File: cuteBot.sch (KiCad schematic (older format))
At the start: 18 parts

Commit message: Añadidos algunos componentes principales
Añadidos los leds. puente en H y pulsador.
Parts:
- removed U?: ATMEGA32U4-MU, QFN44, symbol atmel:ATMEGA32U4-MU
- added C10: 10uF, symbol device:CP_Small
- added C11: 0.01uF, symbol device:C_Small
- added C12, C13, C14, C15, C16: 100nF, symbol device:C_Small
- added C3, C4: 22uF, symbol device:C_Small
- added C5, C6: 22pF, symbol device:C_Small
- added C7: 1uF, symbol device:C_Small
- added C8: 100n, symbol device:C_Small
- added C9: 2.2uF, symbol device:C_Small
- added D3: SS34, symbol device:D_Schottky_Small
- added D4: GREEN, symbol device:LED_Small_ALT
- added D5: RED, symbol device:LED_Small_ALT
- added L1: 22nH, symbol device:L_Small
- added LED1, LED2, LED3, LED4, LED5: WS2812B, LEDs:LED_WS2812B-PLCC4, symbol Worldsemi:WS2812B
- added P4: MOTOR_A, symbol conn:CONN_01X02
- added P5: MOTOR_B, symbol conn:CONN_01X02
- added R10, R15: 10k, symbol device:R_Small
- added R11, R12: 0.2R, symbol device:R_Small
- added R13, R14: 330, symbol device:R_Small
- added R6: 7.5K, symbol device:R_Small
- added R7: 1K, symbol device:R_Small
- added R8, R9: 22R, symbol device:R_Small
- added SW2: SW_Push, symbol Switch:SW_Push
- added U1: ATMEGA32U4-MU, QFN44, symbol atmel:ATMEGA32U4-MU
- added U6: DRV8833RTY, Housings_DFN_QFN:WQFN-16-1EP_4x4mm_Pitch0.65mm, symbol motor_drivers:DRV8833RTY
- added Y1: 16MHz, symbol device:Crystal_Small
- R1: renamed from R?; value 2K -> 4k
- gave numbers to parts that had none: 16
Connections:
- net labels added: 5V, AREF, B1, D+, D-, MOTOR_A_1, MOTOR_A_2, MOTOR_B_1, MOTOR_B_2, NEO, RX_LED, TX_LED, VCP
- wire segments 62 -> 245
- no-connect marks 4 -> 7

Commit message: Añadiendo los componentes, hay algunos errores de footprint
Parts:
- added BZ1: Buzzer, Buzzers_Beepers:PUIAudio_SMT_0825_S_4_R, symbol device:Buzzer
- added C17: 470pF, Capacitors_SMD:C_0603, symbol device:C_Small
- added C18: 2.2uF, Capacitors_SMD:C_0603, symbol device:CP_Small
- added C19, C20: 0.1uF, Capacitors_SMD:C_0603, symbol device:C_Small
- added C21: 10uF, Capacitors_SMD:C_0603, symbol device:C_Small
- added D6: 1N4148, Diodes_SMD:D_MicroMELF, symbol Diode:1N4148
- added P6: CONN_02X03, Connectors:2X3_SMT_POSTS, symbol conn:CONN_02X03
- added Q1: S8050, TO_SOT_Packages_THT:TO-92_Molded_Narrow, symbol Transistor:S8050
- added R16: 100, Resistors_SMD:R_0603, symbol device:R_Small
- added SW3: SW_Push, Buttons_Switches_SMD:SW_SPST_B3U-3000P, symbol Switch:SW_Push
- added U7: JDY-08, JDY-08:JDY-08, symbol jdy-08:JDY-08
- added U8: MIC5219-3.3, TO_SOT_Packages_SMD:SOT-23-5, symbol regul:MIC5219-3.3
- C1, C10, C11, C12, C13, C14, C15, C16, C2, C5, C6, C7, C8, C9: footprint (none) -> Capacitors_SMD:C_0603
- C3, C4: footprint (none) -> Capacitors_SMD:C_1812
- D1, D2, D4, D5: footprint (none) -> LEDs:LED_0603
- D3: footprint (none) -> Diodes_SMD:D_SMA
- L1: footprint (none) -> Inductors_SMD:L_7.3x7.3_H4.5
- LED1, LED2, LED3, LED4, LED5: footprint LEDs:LED_WS2812B-PLCC4 -> LED:LED_SK6812MINI_PLCC4_3.5x3.5mm_P1.75mm
- P1: footprint (none) -> Connectors_USB:USB_Micro-B_Molex-105017-0001
- P2, P3: footprint (none) -> Connectors_TestPoints:Test_Point_Pad_d1.0mm
- P4, P5: footprint (none) -> Connectors_JST:JST_PH_B2B-PH-SM4-TB_02x2.00mm_Straight
- R1, R10, R11, R12, R13, R14, R15, R2, R3, R4, R5, R6, R7, R8, R9: footprint (none) -> Resistors_SMD:R_0603
- SW1: footprint (none) -> Buttons_Switches_SMD:SW_SPDT_PCM12
- SW2: footprint (none) -> Buttons_Switches_SMD:SW_SPST_B3U-3000P
- U1: footprint QFN44 -> Housings_DFN_QFN:QFN-44-1EP_7x7mm_Pitch0.5mm
- U2: footprint (none) -> Housings_SOIC:HTSOP-8-1EP_3.9x4.9mm_Pitch1.27mm_ThermalVias
- U3, U4, U5: footprint (none) -> TO_SOT_Packages_SMD:SOT-23-6
- Y1: footprint (none) -> Crystals:Resonator_7.2x3mm
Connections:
- net labels added: 3.3V, BUZZ, MISO, MOSI, RST, RXD, SCK, TXD
- wire segments 245 -> 302
- no-connect marks 7 -> 25
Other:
- note added: "No conectar las resistencias\na menos que se quiera limitar \nla corriente de los motores"
- moved on the sheet: SW2

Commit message: Footprints correctos
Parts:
- BZ1: footprint Buzzers_Beepers:PUIAudio_SMT_0825_S_4_R -> frizzy_switches:Buzzer-7.5x7.5mm
- P4, P5: footprint Connectors_JST:JST_PH_B2B-PH-SM4-TB_02x2.00mm_Straight -> frizzy_switches:SMD_2pin_Solderpad
- Y1: footprint Crystals:Resonator_7.2x3mm -> Clocks:RESONATOR-SMD-3.2X1.3
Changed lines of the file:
@@
 F 0 "Y1" V 1454 4263 50  0000 R CNN
 F 1 "16MHz" V 1545 4263 50  0000 R CNN
-F 2 "Crystals:Resonator_7.2x3mm" H 1500 4350 50  0001 C CNN
+F 2 "Clocks:RESONATOR-SMD-3.2X1.3" H 1500 4350 50  0001 C CNN
 F 3 "" H 1500 4350 50  0001 C CNN
 	1    1500 4350
@@
 F 0 "P4" H 10728 5541 50  0000 L CNN
 F 1 "MOTOR_A" H 10728 5450 50  0000 L CNN
-F 2 "Connectors_JST:JST_PH_B2B-PH-SM4-TB_02x2.00mm_Straight" H 10650 5500 50  0001 C CNN
+F 2 "frizzy_switches:SMD_2pin_Solderpad" H 10650 5500 50  0001 C CNN
 F 3 "" H 10650 5500 50  0001 C CNN
 	1    10650 5500
@@
 F 0 "P5" H 10727 5841 50  0000 L CNN
 F 1 "MOTOR_B" H 10727 5750 50  0000 L CNN
-F 2 "Connectors_JST:JST_PH_B2B-PH-SM4-TB_02x2.00mm_Straight" H 10650 5800 50  0001 C CNN
+F 2 "frizzy_switches:SMD_2pin_Solderpad" H 10650 5800 50  0001 C CNN
 F 3 "" H 10650 5800 50  0001 C CNN
 	1    10650 5800
@@
 F 0 "BZ1" H 9103 3279 50  0000 L CNN
 F 1 "Buzzer" H 9103 3188 50  0000 L CNN
-F 2 "Buzzers_Beepers:PUIAudio_SMT_0825_S_4_R" V 8925 3350 50  0001 C CNN
+F 2 "frizzy_switches:Buzzer-7.5x7.5mm" V 8925 3350 50  0001 C CNN
 F 3 "" V 8925 3350 50  0001 C CNN
 	1    8950 3250

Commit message: Colocando los componentes
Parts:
- Q1: footprint TO_SOT_Packages_THT:TO-92_Molded_Narrow -> TO_SOT_Packages_SMD:SOT-23
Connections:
- wire segments 302 -> 303
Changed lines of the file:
@@
 F 0 "Q1" H 8941 3696 50  0000 L CNN
 F 1 "S8050" H 8941 3605 50  0000 L CNN
-F 2 "TO_SOT_Packages_THT:TO-92_Molded_Narrow" H 8950 3575 50  0001 L CIN
+F 2 "TO_SOT_Packages_SMD:SOT-23" H 8950 3575 50  0001 L CIN
 F 3 "http://www.unisonic.com.tw/datasheet/S8050.pdf" H 8750 3650 50  0001 L CNN
 	1    8750 3650
@@
 Wire Wire Line
 	1200 3850 1450 3850
+Text GLabel 4050 5050 2    50   Input ~ 0
+BUZZ
+Wire Wire Line
+	3950 5050 4050 5050
 $EndSCHEMATC

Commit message: Colocando los componentes
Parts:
- BZ1: symbol device:Buzzer -> cuteBot-rescue:Buzzer-device
- C1, C11, C12, C13, C14, C15, C16, C17, C19, C2, C20, C21, C3, C4, C5, C6, C7, C8, C9: symbol device:C_Small -> cuteBot-rescue:C_Small-device
- C10, C18: symbol device:CP_Small -> cuteBot-rescue:CP_Small-device
- D1, D2, D4, D5: symbol device:LED_Small_ALT -> cuteBot-rescue:LED_Small_ALT-device
- D3: symbol device:D_Schottky_Small -> cuteBot-rescue:D_Schottky_Small-device
- L1: symbol device:L_Small -> cuteBot-rescue:L_Small-device
- LED1, LED2, LED3, LED4, LED5: symbol Worldsemi:WS2812B -> cuteBot-rescue:WS2812B-Worldsemi
- P1: symbol conn:USB_A -> cuteBot-rescue:USB_A-conn
- P2, P3: symbol conn:CONN_01X01 -> cuteBot-rescue:CONN_01X01-conn
- P4, P5: symbol conn:CONN_01X02 -> cuteBot-rescue:CONN_01X02-conn
- P6: symbol conn:CONN_02X03 -> cuteBot-rescue:CONN_02X03-conn
- Q1: symbol Transistor:S8050 -> cuteBot-rescue:S8050-Transistor
- R1, R10, R11, R12, R13, R14, R15, R16, R2, R3, R4, R5, R6, R7, R8, R9: symbol device:R_Small -> cuteBot-rescue:R_Small-device
- U1: symbol atmel:ATMEGA32U4-MU -> cuteBot-rescue:ATMEGA32U4-MU-atmel
- U2: symbol tp4056:TP4056 -> cuteBot-rescue:TP4056-tp4056
- U3: symbol frizzy_ICs:FS312F-G -> cuteBot-rescue:FS312F-G-frizzy_ICs
- U4: symbol frizzy_ICs:FS8205 -> cuteBot-rescue:FS8205-frizzy_ICs
- U5: symbol frizzy_ICs:MT3608 -> cuteBot-rescue:MT3608-frizzy_ICs
- U6: symbol motor_drivers:DRV8833RTY -> cuteBot-rescue:DRV8833RTY-motor_drivers
- U7: symbol jdy-08:JDY-08 -> cuteBot-rescue:JDY-08-jdy-08
- U8: symbol regul:MIC5219-3.3 -> cuteBot-rescue:MIC5219-3.3-regul
- Y1: symbol device:Crystal_Small -> cuteBot-rescue:Crystal_Small-device

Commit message: Resonador cambiado
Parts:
- removed C5, C6: 22pF, Capacitors_SMD:C_0603, symbol cuteBot-rescue:C_Small-device
- Y1: symbol cuteBot-rescue:Crystal_Small-device -> device:Resonator_Small
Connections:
- net GND: now also Y1.2
- net at U1.16 (XTAL2): now also Y1.3; no longer Y1.2
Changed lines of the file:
@@
 $EndComp
 $Comp
-L cuteBot-rescue:Crystal_Small-device Y1
+L device:Resonator_Small Y1
 U 1 1 5C2CFA66
-P 1500 4350
-F 0 "Y1" V 1454 4263 50  0000 R CNN
-F 1 "16MHz" V 1545 4263 50  0000 R CNN
-F 2 "Clocks:RESONATOR-SMD-3.2X1.3" H 1500 4350 50  0001 C CNN
-F 3 "" H 1500 4350 50  0001 C CNN
-	1    1500 4350
-	0    1    1    0
-$EndComp
-$Comp
-L cuteBot-rescue:C_Small-device C5
-U 1 1 5C2CFD53
-P 1300 4200
-F 0 "C5" V 1071 4200 50  0000 C CNN
-F 1 "22pF" V 1162 4200 50  0000 C CNN
-F 2 "Capacitors_SMD:C_0603" H 1300 4200 50  0001 C CNN
-F 3 "" H 1300 4200 50  0001 C CNN
-	1    1300 4200
-	0    1    1    0
-$EndComp
-$Comp
-L cuteBot-rescue:C_Small-device C6
-U 1 1 5C2CFF48
-P 1300 4500
-F 0 "C6" V 1437 4500 50  0000 C CNN
-F 1 "22pF" V 1528 4500 50  0000 C CNN
-F 2 "Capacitors_SMD:C_0603" H 1300 4500 50  0001 C CNN
-F 3 "" H 1300 4500 50  0001 C CNN
-	1    1300 4500
-	0    1    1    0
-$EndComp
-Wire Wire Line
-	1400 4200 1500 4200
-Wire Wire Line
-	1500 4200 1500 4250
+P 1400 4350
+F 0 "Y1" V 1250 4200 50  0000 R CNN
+F 1 "16MHz" V 1600 4400 50  0000 R CNN
+F 2 "Clocks:RESONATOR-SMD-3.2X1.3" H 1400 4350 50  0001 C CNN
+F 3 "" H 1400 4350 50  0001 C CNN
+	1    1400 4350
+	0    1    1    0
+$EndComp
 Wire Wire Line
 	1700 4250 1500 4250
-Connection ~ 1500 4250
 Wire Wire Line
 	1500 4450 1700 4450
-Wire Wire Line
-	1500 4450 1500 4500
-Wire Wire Line
-	1500 4500 1400 4500
-Connection ~ 1500 4450
-Wire Wire Line
-	1200 4200 1100 4200
-Wire Wire Line
-	1100 4200 1100 4350
-Wire Wire Line
-	1100 4500 1200 4500
-Wire Wire Line
-	1100 4350 1050 4350
-Connection ~ 1100 4350
-Wire Wire Line
-	1100 4350 1100 4500
 $Comp
 L power:GND #PWR011
@@
 Wire Wire Line
 	3950 5050 4050 5050
+Wire Wire Line
+	1050 4350 1200 4350
 $EndSCHEMATC

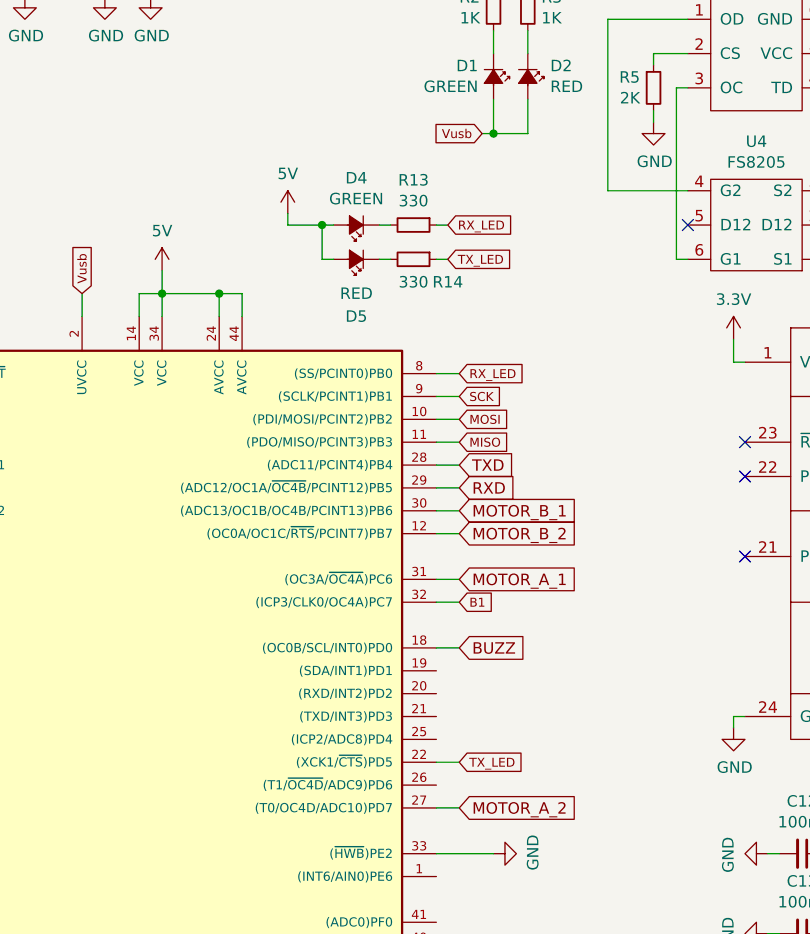
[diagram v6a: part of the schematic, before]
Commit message: Leds RX/TX eliminados
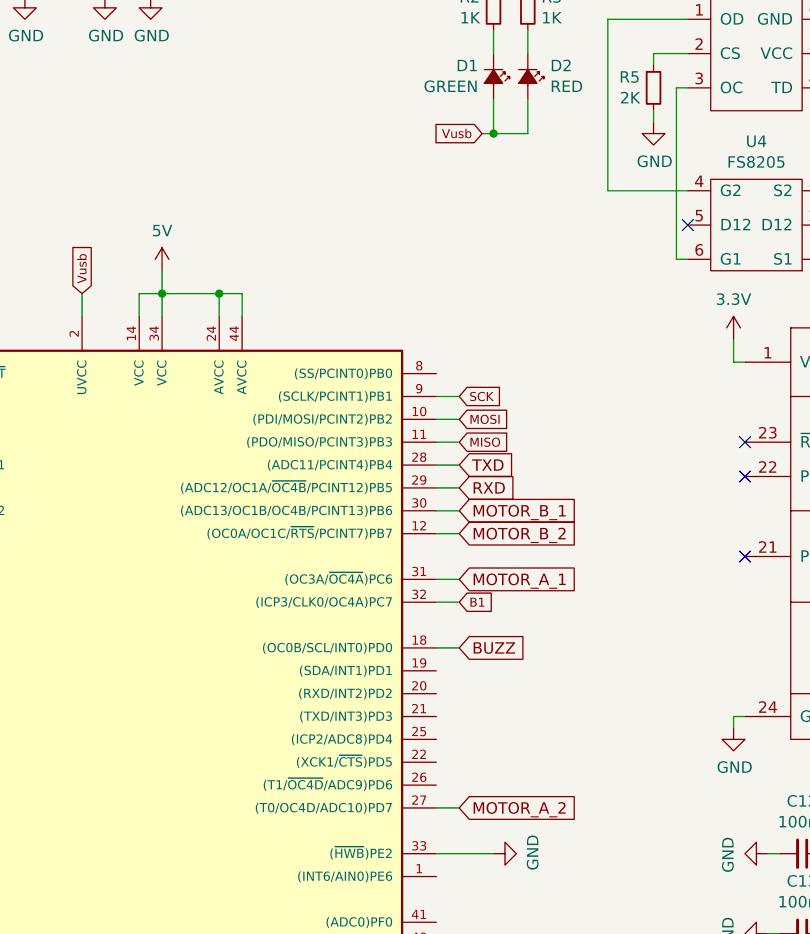
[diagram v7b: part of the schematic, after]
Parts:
- removed D4: GREEN, LEDs:LED_0603, symbol cuteBot-rescue:LED_Small_ALT-device
- removed D5: RED, LEDs:LED_0603, symbol cuteBot-rescue:LED_Small_ALT-device
- removed R13, R14: 330, Resistors_SMD:R_0603, symbol cuteBot-rescue:R_Small-device
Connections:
- net RX_LED: no longer names the net of U1.8 ((SS/PCINT0)PB0)
- net TX_LED: no longer names the net of U1.22 ((XCK1/~CTS~)PD5)
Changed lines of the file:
@@
 Wire Wire Line
 	3950 4850 4050 4850
-Wire Wire Line
-	3950 3850 4050 3850
-Wire Wire Line
-	3950 5550 4050 5550
-Text GLabel 4050 3850 2    39   Input ~ 0
-RX_LED
-Text GLabel 4050 5550 2    39   Input ~ 0
-TX_LED
-Text GLabel 4000 3200 2    39   Input ~ 0
-RX_LED
-Text GLabel 4000 3350 2    39   Input ~ 0
-TX_LED
-$Comp
-L cuteBot-rescue:R_Small-device R13
-U 1 1 5C5F9433
-P 3850 3200
-F 0 "R13" V 3654 3200 50  0000 C CNN
-F 1 "330" V 3745 3200 50  0000 C CNN
-F 2 "Resistors_SMD:R_0603" H 3850 3200 50  0001 C CNN
-F 3 "" H 3850 3200 50  0001 C CNN
-	1    3850 3200
-	0    1    1    0
-$EndComp
-$Comp
-L cuteBot-rescue:R_Small-device R14
-U 1 1 5C5F9772
-P 3850 3350
-F 0 "R14" V 3950 3500 50  0000 C CNN
-F 1 "330" V 3950 3350 50  0000 C CNN
-F 2 "Resistors_SMD:R_0603" H 3850 3350 50  0001 C CNN
-F 3 "" H 3850 3350 50  0001 C CNN
-	1    3850 3350
-	0    1    1    0
-$EndComp
-Wire Wire Line
-	3950 3200 4000 3200
-Wire Wire Line
-	3950 3350 4000 3350
-$Comp
-L cuteBot-rescue:LED_Small_ALT-device D4
-U 1 1 5C6179F6
-P 3600 3200
-F 0 "D4" H 3600 2995 50  0000 C CNN
-F 1 "GREEN" H 3600 3086 50  0000 C CNN
-F 2 "LEDs:LED_0603" V 3600 3200 50  0001 C CNN
-F 3 "~" V 3600 3200 50  0001 C CNN
-	1    3600 3200
-	-1   0    0    1
-$EndComp
-$Comp
-L cuteBot-rescue:LED_Small_ALT-device D5
-U 1 1 5C617D36
-P 3600 3350
-F 0 "D5" H 3600 3600 50  0000 C CNN
-F 1 "RED" H 3600 3500 50  0000 C CNN
-F 2 "LEDs:LED_0603" V 3600 3350 50  0001 C CNN
-F 3 "~" V 3600 3350 50  0001 C CNN
-	1    3600 3350
-	-1   0    0    1
-$EndComp
-Wire Wire Line
-	3700 3200 3750 3200
-Wire Wire Line
-	3700 3350 3750 3350
-Wire Wire Line
-	3450 3200 3450 3350
-Wire Wire Line
-	3450 3350 3500 3350
-Wire Wire Line
-	3450 3200 3500 3200
-$Comp
-L cuteBot-rescue:5V-SparkFun-Aesthetics #SUPPLY07
-U 1 1 5C654626
-P 3300 3150
-F 0 "#SUPPLY07" H 3300 3150 50  0001 L BNN
-F 1 "5V" H 3300 3324 50  0000 C CNN
-F 2 "" H 3300 3150 50  0001 C CNN
-F 3 "" H 3300 3150 50  0001 C CNN
-	1    3300 3150
-	1    0    0    -1
-$EndComp
-Wire Wire Line
-	3300 3200 3450 3200
-Connection ~ 3450 3200
-Wire Wire Line
-	3300 3150 3300 3200
 $Comp
 L cuteBot-rescue:JDY-08-jdy-08 U7

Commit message: Errores corregidos.
Vias que provocaban un corto, pinout del Q1 erróneo  y flag de los neopixel no conectado al micro.
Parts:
- D6: symbol Diode:1N4148 -> cuteBot-rescue:1N4148-Diode
- SW1: symbol Switch:SW_SPDT -> cuteBot-rescue:SW_SPDT-Switch
- SW2, SW3: symbol Switch:SW_Push -> cuteBot-rescue:SW_Push-Switch
- Y1: symbol device:Resonator_Small -> cuteBot-rescue:Resonator_Small-device
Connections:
- net NEO: now also U1.19 ((SDA/INT1)PD1)
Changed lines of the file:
@@
 $EndComp
 $Comp
-L power:GND #PWR01
+L cuteBot-rescue:GND-power #PWR01
 U 1 1 5C1699ED
 P 1300 2200
@@
 $EndComp
 $Comp
-L power:GND #PWR02
+L cuteBot-rescue:GND-power #PWR02
 U 1 1 5C169A0B
 P 1800 2200
@@
 $EndComp
 $Comp
-L power:GND #PWR03
+L cuteBot-rescue:GND-power #PWR03
 U 1 1 5C16ACDD
 P 2150 2200
@@
 	2150 2200 2150 2150
 $Comp
-L power:GND #PWR04
+L cuteBot-rescue:GND-power #PWR04
 U 1 1 5C16AEC0
 P 2500 2200
@@
 	2150 1600 2150 1900
 $Comp
-L power:GND #PWR05
+L cuteBot-rescue:GND-power #PWR05
 U 1 1 5C16B206
 P 2700 2200
@@
 Connection ~ 4200 2800
 $Comp
-L Switch:SW_SPDT SW1
+L cuteBot-rescue:SW_SPDT-Switch SW1
 U 1 1 5C16E564
 P 6450 1500
@@
 	4700 2300 5050 2300
 $Comp
-L power:GND #PWR06
+L cuteBot-rescue:GND-power #PWR06
 U 1 1 5C1724AF
 P 4900 2750
@@
 	5000 2600 5000 3350
 $Comp
-L power:GND #PWR07
+L cuteBot-rescue:GND-power #PWR07
 U 1 1 5C175BAC
 P 5700 3400
@@
 	7400 1650 7450 1650
 $Comp
-L power:GND #PWR08
+L cuteBot-rescue:GND-power #PWR08
 U 1 1 5C16E214
 P 7700 2050
@@
 Connection ~ 8500 1750
 $Comp
-L power:GND #PWR09
+L cuteBot-rescue:GND-power #PWR09
 U 1 1 5C182A81
 P 8500 2100
@@
 Connection ~ 8500 1250
 $Comp
-L power:GND #PWR010
+L cuteBot-rescue:GND-power #PWR010
 U 1 1 5C187DD9
 P 8850 2100
@@
 	1700 1800 1800 1800
 $Comp
-L power:GND #PWR015
+L cuteBot-rescue:GND-power #PWR015
 U 1 1 5C199DCA
 P 2850 7250
@@
 	2800 7100 2850 7100
 $Comp
-L power:GND #PWR014
+L cuteBot-rescue:GND-power #PWR014
 U 1 1 5C1A64F3
 P 2450 7250
@@
 	3950 5950 4200 5950
 $Comp
-L power:GND #PWR016
+L cuteBot-rescue:GND-power #PWR016
 U 1 1 5C1AC2E2
 P 4200 5950
@@
 $EndComp
 $Comp
-L device:Resonator_Small Y1
+L cuteBot-rescue:Resonator_Small-device Y1
 U 1 1 5C2CFA66
 P 1400 4350
@@
 	1500 4450 1700 4450
 $Comp
-L power:GND #PWR011
+L cuteBot-rescue:GND-power #PWR011
 U 1 1 5C2E3814
 P 1050 4350
@@
 $EndComp
 $Comp
-L power:GND #PWR012
+L cuteBot-rescue:GND-power #PWR012
 U 1 1 5C2F592E
 P 1600 5850
@@
 $EndComp
 $Comp
-L power:GND #PWR013
+L cuteBot-rescue:GND-power #PWR013
 U 1 1 5C300FD5
 P 1650 6550
@@
 NoConn ~ 10200 5300
 $Comp
-L power:GND #PWR019
+L cuteBot-rescue:GND-power #PWR019
 U 1 1 5C33D266
 P 9550 6150
@@
 	9700 4650 9700 4600
 $Comp
-L power:GND #PWR020
+L cuteBot-rescue:GND-power #PWR020
 U 1 1 5C37A124
 P 9700 4350
@@
 	10200 4650 10200 4350
 $Comp
-L power:GND #PWR021
+L cuteBot-rescue:GND-power #PWR021
 U 1 1 5C3C4FED
 P 10350 4650
@@
 	6600 6050 6600 6400
 $Comp
-L power:GND #PWR017
+L cuteBot-rescue:GND-power #PWR017
 U 1 1 5C493FF5
 P 6600 7600
@@
 Connection ~ 5700 7400
 $Comp
-L power:GND #PWR026
+L cuteBot-rescue:GND-power #PWR026
 U 1 1 5C50E7B8
 P 5400 7400
@@
 	5400 7400 5450 7400
 $Comp
-L power:GND #PWR025
+L cuteBot-rescue:GND-power #PWR025
 U 1 1 5C51B573
 P 5400 7000
@@
 	5400 7000 5450 7000
 $Comp
-L power:GND #PWR024
+L cuteBot-rescue:GND-power #PWR024
 U 1 1 5C5283D6
 P 5400 6650
@@
 	5650 6300 5700 6300
 $Comp
-L power:GND #PWR023
+L cuteBot-rescue:GND-power #PWR023
 U 1 1 5C55CF5B
 P 5400 6300
@@
 	5400 6300 5450 6300
 $Comp
-L power:GND #PWR022
+L cuteBot-rescue:GND-power #PWR022
 U 1 1 5C56A50E
 P 5400 5950
@@
 	5400 5950 5450 5950
 $Comp
-L Switch:SW_Push SW2
+L cuteBot-rescue:SW_Push-Switch SW2
 U 1 1 5C5869BB
 P 10600 3050
@@
 $EndComp
 $Comp
-L power:GND #PWR027
+L cuteBot-rescue:GND-power #PWR027
 U 1 1 5C586C51
 P 10600 3300
@@
 $EndComp
 $Comp
-L power:GND #PWR028
+L cuteBot-rescue:GND-power #PWR028
 U 1 1 5C50B398
 P 5250 5400
@@
 Connection ~ 9600 1250
 $Comp
-L power:GND #PWR029
+L cuteBot-rescue:GND-power #PWR029
 U 1 1 5C53DBA7
 P 10000 1700
@@
 	10450 1350 10450 1450
 $Comp
-L power:GND #PWR030
+L cuteBot-rescue:GND-power #PWR030
 U 1 1 5C55FC08
 P 10450 1700
@@
 Connection ~ 10750 1250
 $Comp
-L power:GND #PWR031
+L cuteBot-rescue:GND-power #PWR031
 U 1 1 5C5936C6
 P 10750 1700
@@
 	8850 3050 8850 3150
 $Comp
-L power:GND #PWR018
+L cuteBot-rescue:GND-power #PWR018
 U 1 1 5C856F7D
 P 8850 3950
@@
 	8850 3850 8850 3950
 $Comp
-L Diode:1N4148 D6
+L cuteBot-rescue:1N4148-Diode D6
 U 1 1 5C86AC7E
 P 8750 3250
@@
 	7650 3100 7650 3050
 $Comp
-L power:GND #PWR032
+L cuteBot-rescue:GND-power #PWR032
 U 1 1 5C719E40
 P 7650 3350
@@
 	7600 3200 7650 3200
 $Comp
-L power:GND #PWR034
+L cuteBot-rescue:GND-power #PWR034
 U 1 1 5C747463
 P 8650 5250
@@
 	700  3850 800  3850
 $Comp
-L power:GND #PWR033
+L cuteBot-rescue:GND-power #PWR033
 U 1 1 5C80B676
 P 700 3950
@@
 Connection ~ 4000 7050
 $Comp
-L power:GND #PWR035
+L cuteBot-rescue:GND-power #PWR035
 U 1 1 5C8FDA07
 P 4000 7450
@@
 $EndComp
 $Comp
-L Switch:SW_Push SW3
+L cuteBot-rescue:SW_Push-Switch SW3
 U 1 1 5C9028BA
 P 1000 3850
@@
 Wire Wire Line
 	1050 4350 1200 4350
+Text GLabel 4050 5150 2    39   Input ~ 0
+NEO
+Wire Wire Line
+	3950 5150 4050 5150
 $EndSCHEMATC
